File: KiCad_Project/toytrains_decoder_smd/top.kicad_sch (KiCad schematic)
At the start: 43 parts, among them IC1 TLE5206-2G, Q1 BSS138, Q2 BSS138, Q3 BSS138, Q4 BSS138, Q5 BSS138, Q6 BSS138

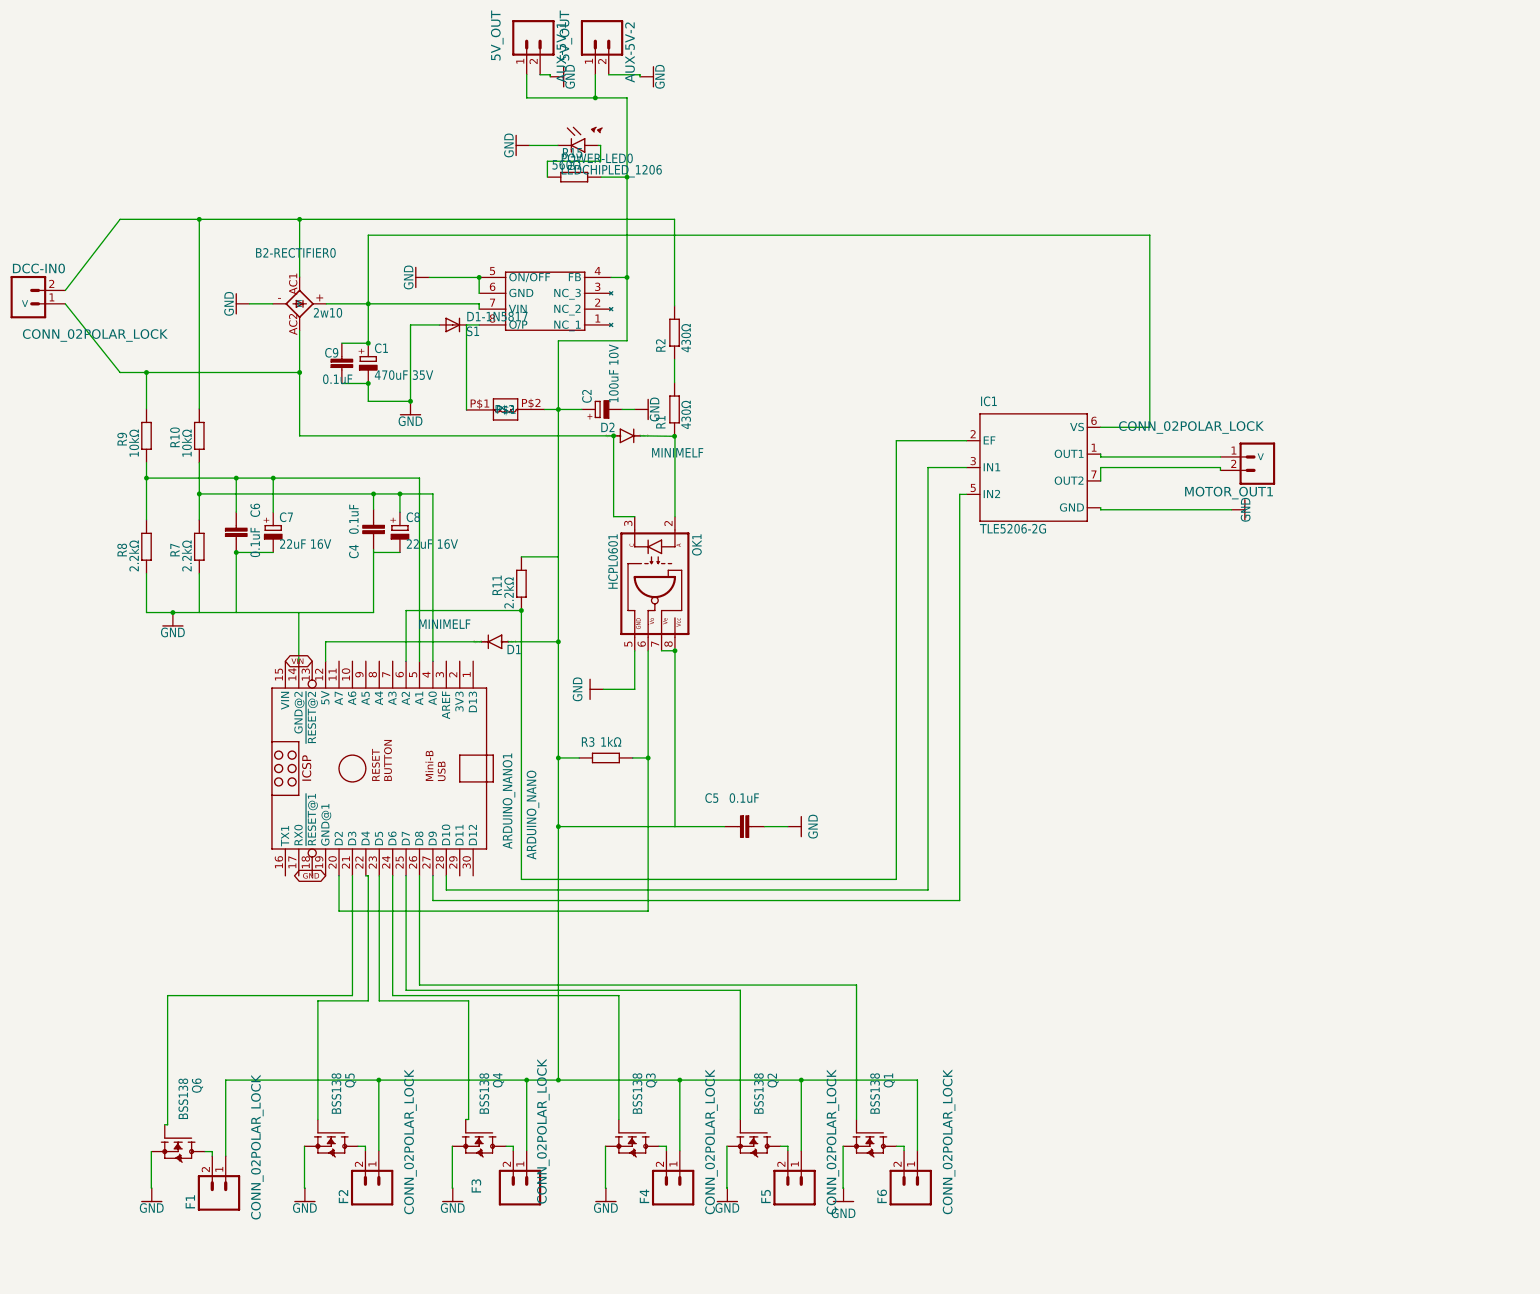
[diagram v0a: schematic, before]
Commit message: KiCad: add rev2 schematic and update PCB design files
- Add CAB_decoder_SMD_rev2.kicad_sch (PCB revision in progress)
- Add eagle import symbol library and sym-lib-table
- Add top.kicad_sch sheet
- Update main schematic and project files
- Gitignore KiCad lock files, backups, .history, .vscode, .claude

Co-Authored-By: Claude Sonnet 4.6 <noreply@anthropic.com>
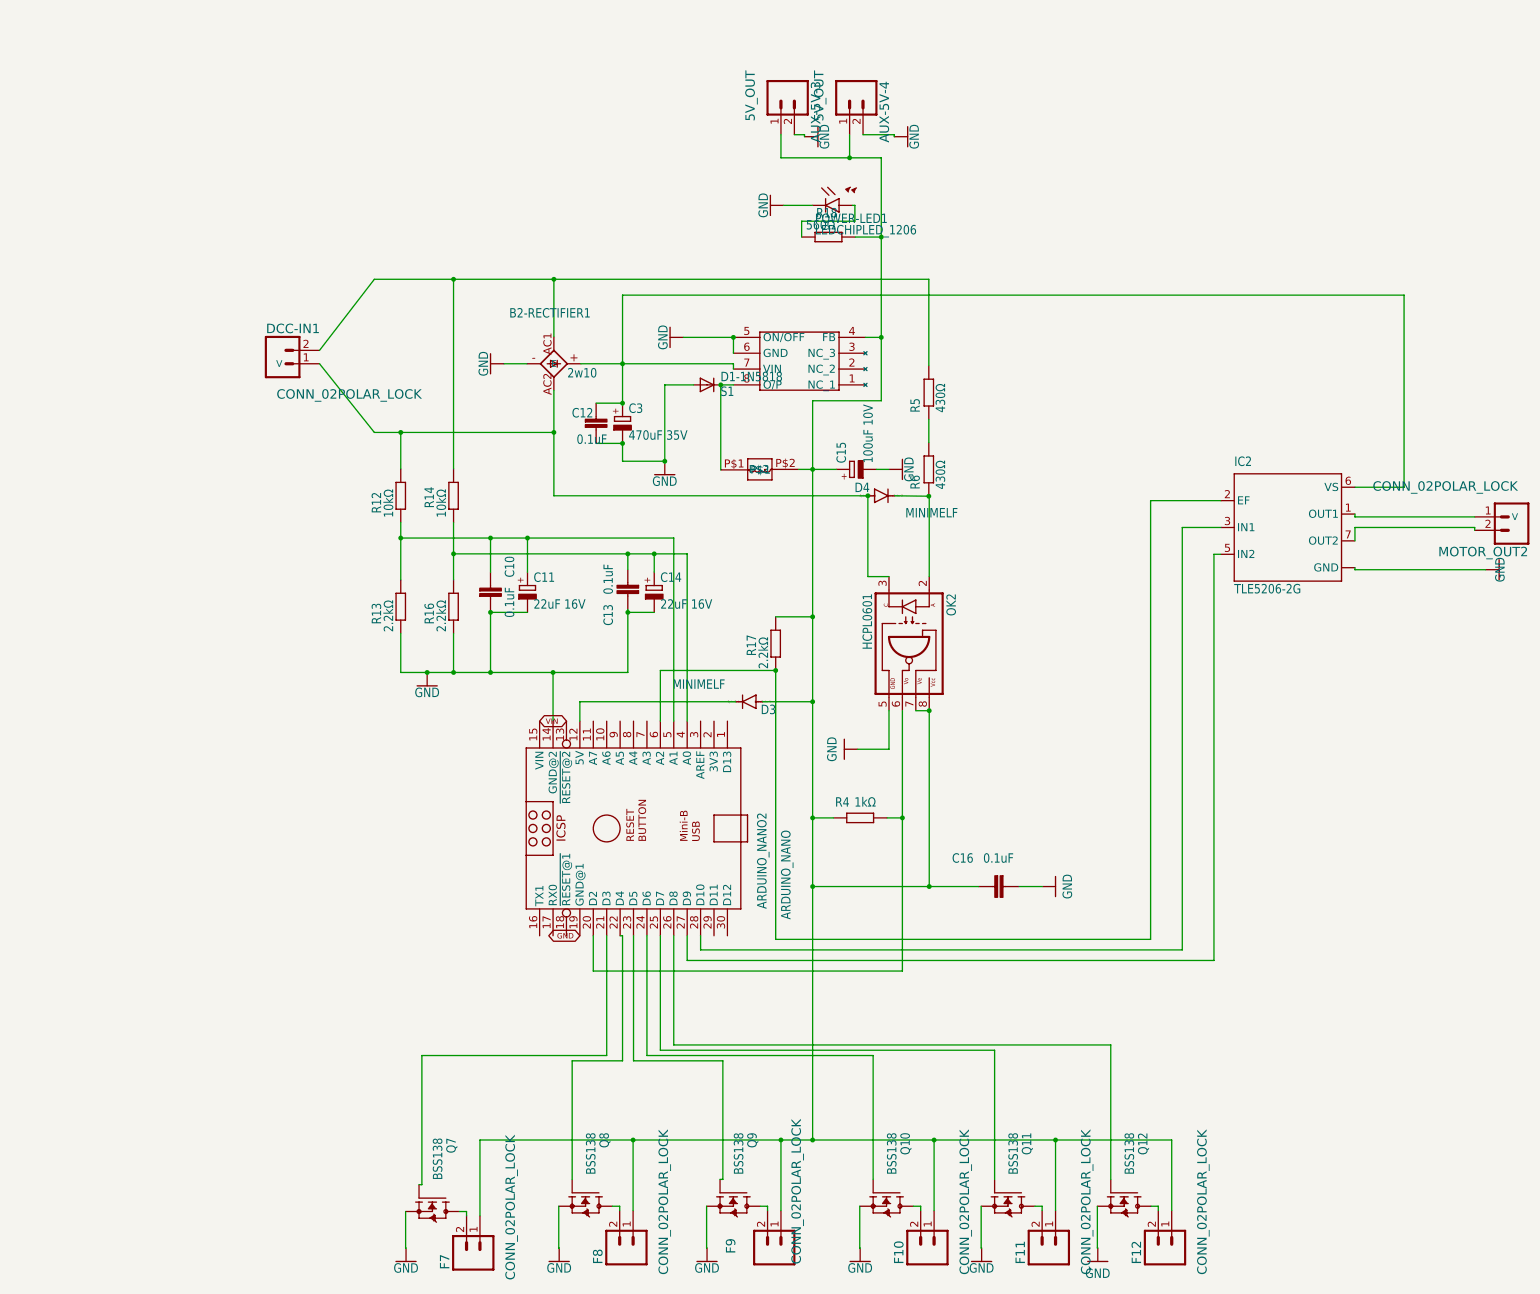
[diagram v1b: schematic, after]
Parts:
- removed ARDUINO_NANO1: ARDUINO_NANO, toytrains_decoder_smd:ARDUINO_NANO, symbol toytrains_decoder_smd-eagle-import:ArduinoNanoV30_ARDUINO_NANO
- removed AUX-5V-1, AUX-5V-2: 5V_OUT, toytrains_decoder_smd:MOLEX-1X2_LOCK, symbol toytrains_decoder_smd-eagle-import:SparkFun-Connectors_513_CONN_02POLAR_LOCK
- removed B2-RECTIFIER0: 2w10, toytrains_decoder_smd:1KAB, symbol toytrains_decoder_smd-eagle-import:rectifier_336_1KAB
- removed C1: 470uF 35V, toytrains_decoder_smd:153CLV-1014, symbol toytrains_decoder_smd-eagle-import:rcl_334_CPOL-EU153CLV-1014
- removed C2: 100uF 10V, toytrains_decoder_smd:153CLV-0605, symbol toytrains_decoder_smd-eagle-import:rcl_334_CPOL-EU153CLV-0605
- removed C4, C5, C6, C9: 0.1uF, toytrains_decoder_smd:C1206, symbol toytrains_decoder_smd-eagle-import:rcl_334_C-EUC1206
- removed C7, C8: 22uF 16V, toytrains_decoder_smd:153CLV-0405, symbol toytrains_decoder_smd-eagle-import:rcl_334_CPOL-EU153CLV-0405
- removed D1, D2: MINIMELF, toytrains_decoder_smd:MINIMELF, symbol toytrains_decoder_smd-eagle-import:diode_210_DIODE-MINIMELF
- removed D1-1N5817: S1, toytrains_decoder_smd:DO214AC, symbol toytrains_decoder_smd-eagle-import:s1x_10_S1
- removed DCC-IN0, F1, F2, F3, F4, F5, F6, MOTOR_OUT1: CONN_02POLAR_LOCK, toytrains_decoder_smd:MOLEX-1X2_LOCK, symbol toytrains_decoder_smd-eagle-import:SparkFun-Connectors_513_CONN_02POLAR_LOCK
- removed IC1: TLE5206-2G, toytrains_decoder_smd:P-TO263-7-1, symbol toytrains_decoder_smd-eagle-import:HBridge_TLE5206-2G
- removed OK1: HCPL0601, toytrains_decoder_smd:SOIC08, symbol toytrains_decoder_smd-eagle-import:optocoupler_320_HCPL0601
- removed POWER-LED0: LEDCHIPLED_1206, toytrains_decoder_smd:CHIPLED_1206, symbol toytrains_decoder_smd-eagle-import:led_259_LEDCHIPLED_1206
- removed Q1, Q2, Q3, Q4, Q5, Q6: BSS138, toytrains_decoder_smd:SOT23, symbol toytrains_decoder_smd-eagle-import:bss138_10_BSS138
- removed R1, R2: 430Ω, toytrains_decoder_smd:R2512, symbol toytrains_decoder_smd-eagle-import:rcl_334_R-EU_R2512
- removed R10, R9: 10kΩ, toytrains_decoder_smd:R1206, symbol toytrains_decoder_smd-eagle-import:rcl_334_R-EU_R1206
- removed R11, R7, R8: 2.2kΩ, toytrains_decoder_smd:R1206, symbol toytrains_decoder_smd-eagle-import:rcl_334_R-EU_R1206
- removed R15: 560Ω, toytrains_decoder_smd:R1206, symbol toytrains_decoder_smd-eagle-import:rcl_334_R-EU_R1206
- removed R3: 1kΩ, toytrains_decoder_smd:R1206, symbol toytrains_decoder_smd-eagle-import:rcl_334_R-EU_R1206
- removed U$1: LM2594, toytrains_decoder_smd:SOIC8, symbol toytrains_decoder_smd-eagle-import:LM2594_LM2594
- removed U$2: L-CD54, toytrains_decoder_smd:L_CD54, symbol toytrains_decoder_smd-eagle-import:Inductor_L-CD54
- added ARDUINO_NANO2: ARDUINO_NANO, toytrains_decoder_smd:ARDUINO_NANO, symbol toytrains_decoder_smd-eagle-import:ArduinoNanoV30_ARDUINO_NANO
- added AUX-5V-3, AUX-5V-4: 5V_OUT, toytrains_decoder_smd:MOLEX-1X2_LOCK, symbol toytrains_decoder_smd-eagle-import:SparkFun-Connectors_513_CONN_02POLAR_LOCK
- added B2-RECTIFIER1: 2w10, toytrains_decoder_smd:1KAB, symbol toytrains_decoder_smd-eagle-import:rectifier_336_1KAB
- added C10, C12, C13, C16: 0.1uF, toytrains_decoder_smd:C1206, symbol toytrains_decoder_smd-eagle-import:rcl_334_C-EUC1206
- added C11, C14: 22uF 16V, toytrains_decoder_smd:153CLV-0405, symbol toytrains_decoder_smd-eagle-import:rcl_334_CPOL-EU153CLV-0405
- added C15: 100uF 10V, toytrains_decoder_smd:153CLV-0605, symbol toytrains_decoder_smd-eagle-import:rcl_334_CPOL-EU153CLV-0605
- added C3: 470uF 35V, toytrains_decoder_smd:153CLV-1014, symbol toytrains_decoder_smd-eagle-import:rcl_334_CPOL-EU153CLV-1014
- added D1-1N5818: S1, toytrains_decoder_smd:DO214AC, symbol toytrains_decoder_smd-eagle-import:s1x_10_S1
- added D3, D4: MINIMELF, toytrains_decoder_smd:MINIMELF, symbol toytrains_decoder_smd-eagle-import:diode_210_DIODE-MINIMELF
- added DCC-IN1, F10, F11, F12, F7, F8, F9, MOTOR_OUT2: CONN_02POLAR_LOCK, toytrains_decoder_smd:MOLEX-1X2_LOCK, symbol toytrains_decoder_smd-eagle-import:SparkFun-Connectors_513_CONN_02POLAR_LOCK
- added IC2: TLE5206-2G, toytrains_decoder_smd:P-TO263-7-1, symbol toytrains_decoder_smd-eagle-import:HBridge_TLE5206-2G
- added OK2: HCPL0601, toytrains_decoder_smd:SOIC08, symbol toytrains_decoder_smd-eagle-import:optocoupler_320_HCPL0601
- added POWER-LED1: LEDCHIPLED_1206, toytrains_decoder_smd:CHIPLED_1206, symbol toytrains_decoder_smd-eagle-import:led_259_LEDCHIPLED_1206
- added Q10, Q11, Q12, Q7, Q8, Q9: BSS138, toytrains_decoder_smd:SOT23, symbol toytrains_decoder_smd-eagle-import:bss138_10_BSS138
- added R12, R14: 10kΩ, toytrains_decoder_smd:R1206, symbol toytrains_decoder_smd-eagle-import:rcl_334_R-EU_R1206
- added R13, R16, R17: 2.2kΩ, toytrains_decoder_smd:R1206, symbol toytrains_decoder_smd-eagle-import:rcl_334_R-EU_R1206
- added R18: 560Ω, toytrains_decoder_smd:R1206, symbol toytrains_decoder_smd-eagle-import:rcl_334_R-EU_R1206
- added R4: 1kΩ, toytrains_decoder_smd:R1206, symbol toytrains_decoder_smd-eagle-import:rcl_334_R-EU_R1206
- added R5, R6: 430Ω, toytrains_decoder_smd:R2512, symbol toytrains_decoder_smd-eagle-import:rcl_334_R-EU_R2512
- added U$3: L-CD54, toytrains_decoder_smd:L_CD54, symbol toytrains_decoder_smd-eagle-import:Inductor_L-CD54
- added U$4: LM2594, toytrains_decoder_smd:SOIC8, symbol toytrains_decoder_smd-eagle-import:LM2594_LM2594
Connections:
- net GND: now also ARDUINO_NANO2.14 (GND@2), ARDUINO_NANO2.19 (GND@1), AUX-5V-3.2, AUX-5V-4.2, B2-RECTIFIER1.-, C10.2, C11.-, C12.2, C13.1, C14.-, C15.-, C16.2, C3.-, D1-1N5818.A, IC2.4 (GND), IC2.8 (GND), OK2.5 (GND), POWER-LED1.C, Q10.2 (S), Q11.2 (S), Q12.2 (S), Q7.2 (S), Q8.2 (S), Q9.2 (S), R13.2, R16.2, U$4.5 (ON/OFF), U$4.6 (GND)
- net VIN: now also ARDUINO_NANO2.15 (VIN)
- new net: AUX-5V-3.1, AUX-5V-4.1, C15.+, C16.1, D3.A, F10.1, F11.1, F12.1, F7.1, F8.1, F9.1, OK2.7 (VE), OK2.8 (VCC), R17.1, R18.1, R4.2, U$3.P$2, U$4.4 (FB)
- new net: F9.2, Q9.3 (D)
- new net: F11.2, Q11.3 (D)
- new net: ARDUINO_NANO2.4 (A0), C13.2, C14.+, R14.2, R16.1
- new net: D1-1N5818.C, U$3.P$1, U$4.8 (O/P)
- new net: ARDUINO_NANO2.5 (A1), C10.1, C11.+, R12.2, R13.1
- new net: ARDUINO_NANO2.12 (5V), D3.C
- new net: ARDUINO_NANO2.20 (D2), OK2.6 (VO), R4.1
- new net: ARDUINO_NANO2.21 (D3), Q7.1 (G)
- new net: ARDUINO_NANO2.22 (D4), Q8.1 (G)
- new net: ARDUINO_NANO2.23 (D5), Q9.1 (G)
- new net: ARDUINO_NANO2.24 (D6), Q10.1 (G)
- new net: ARDUINO_NANO2.25 (D7), Q11.1 (G)
- new net: ARDUINO_NANO2.26 (D8), Q12.1 (G)
- new net: ARDUINO_NANO2.27 (D9), IC2.5 (IN2)
- new net: ARDUINO_NANO2.28 (D10), IC2.3 (IN1)
- new net: ARDUINO_NANO2.6 (A2), IC2.2 (EF), R17.2
- new net: D4.C, OK2.2 (A), R6.1
- new net: B2-RECTIFIER1.AC2, D4.A, DCC-IN1.1, OK2.3 (C), R12.1
- new net: B2-RECTIFIER1.+, C12.1, C3.+, IC2.6 (VS), U$4.7 (VIN)
- new net: B2-RECTIFIER1.AC1, DCC-IN1.2, R14.1, R5.2
- new net: IC2.1 (OUT1), MOTOR_OUT2.1
- new net: IC2.7 (OUT2), MOTOR_OUT2.2
- new net: F7.2, Q7.3 (D)
- new net: F8.2, Q8.3 (D)
- new net: R5.1, R6.2
- new net: F12.2, Q12.3 (D)
- new net: F10.2, Q10.3 (D)
- new net: POWER-LED1.A, R18.2
